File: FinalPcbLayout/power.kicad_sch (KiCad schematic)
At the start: 33 parts, among them Q1 NMOS, U4 AMS1117-3.3

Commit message: Part Finalization
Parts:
- added D4, D5: D_Schottky, symbol Device:D_Schottky
- added D7: RED, symbol Device:LED
- added J3: Barrel_Jack, Connector_BarrelJack:BarrelJack_GCT_DCJ200-10-A_Horizontal, symbol Connector:Barrel_Jack
- added Q4, Q5: PMOS, symbol Simulation_SPICE:PMOS
- added R23, R24: 10k, symbol Device:R_Small
- added R25: 100, symbol Device:R_Small
- D1: cost (none) -> .89; digikey_pn (none) -> SL42-E3/57TGITR-ND
- Q1: cost (none) -> .48; digikey_pn (none) -> 296-37193-6-ND
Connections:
- net +5V: now also D7.2 (A); no longer C1.2, C9.2, L1.1, U5.1 (BIAS), U5.12 (UVLO_)
- net GND: now also J3.2, R23.2, R24.2, R25.2
- net USB_Vin: now also Q4.1 (D); no longer C16.1, R13.1, U3.1 (PS/SYNC), U3.12 (VIN), U3.13 (VIN)
- new net: D7.1 (K), R25.1
- new net: D5.2 (A), Q4.2 (G), R24.1
- new net: D4.2 (A), Q5.2 (G), R23.1
- new net: J3.1, Q5.1 (D)
- new net V_in: C1.2, C16.1, C9.2, D4.1 (K), D5.1 (K), L1.1, Q4.3 (S), Q5.3 (S), R13.1, U3.1 (PS/SYNC), U3.12 (VIN), U3.13 (VIN), U5.1 (BIAS), U5.12 (UVLO_)
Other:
- moved on the sheet: C1, C10, C11, C2, C3, C4, C5, C6, C7, C8, C9, D1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

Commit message: Sim Disabled
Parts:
- C1, C10, C11, C16, C17, C18, C19, C2, C3, C4, C5, C6, C7, C8, C9, D1, D4, D5, D7, J3, L1, L2, Q1, Q4, Q5, R1, R10, R11, R12, R13, R2, R23, R24, R25, R3, R4, R5, R6, R7, U3, U4, U5: Cost (none) -> 0
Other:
- moved on the sheet: C10, C11, U4

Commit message: Update schematic with footprints for power delivery
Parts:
- C10, C16, C18, C19, C6: footprint Capacitor_SMD:C_0603_1608Metric -> Capacitor_SMD:C_0805_2012Metric
- C5: footprint Capacitor_SMD:C_0603_1608Metric -> Capacitor_SMD:C_0201_0603Metric
- C9: footprint Capacitor_SMD:C_0603_1608Metric -> Capacitor_SMD:C_0805_2012Metric; Cost 0 -> (uuid fabb1e82-3a32-4eed-b578-540d99c03e17)
- R3, R4: footprint Resistor_SMD:R_0603_1608Metric -> Resistor_SMD:R_1206_3216Metric
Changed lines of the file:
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@@
       (effects (font (size 1.27 1.27)) hide)
     )
-    (pin "2")
-    (pin "1")
+    (pin "1")
+    (pin "2")
     (instances
       (project "FinalPcbLayout"
@@
       (effects (font (size 1.27 1.27)) hide)
     )
-    (property "Datasheet" "~" (at 97.79 53.34 0)
+    (property "Datasheet" "" (at 97.79 53.34 0)
       (effects (font (size 1.27 1.27)) hide)
     )
@@
       (effects (font (size 1.27 1.27)) hide)
     )
+    (pin "1")
+    (pin "2")
     (pin "3")
-    (pin "1")
-    (pin "2")
     (instances
       (project "FinalPcbLayout"
@@
       (effects (font (size 1.27 1.27)) hide)
     )
-    (pin "2")
-    (pin "1")
+    (pin "1")
+    (pin "2")
     (instances
       (project "FinalPcbLayout"
@@
       (effects (font (size 1.27 1.27)) (justify right))
     )
-    (property "Footprint" "Resistor_SMD:R_0603_1608Metric" (at 217.424 78.486 90)
+    (property "Footprint" "Resistor_SMD:R_1206_3216Metric" (at 217.424 78.486 90)
       (effects (font (size 1.27 1.27)) hide)
     )
@@
       (effects (font (size 1.27 1.27)) (justify right))
     )
-    (property "Footprint" "Capacitor_SMD:C_0603_1608Metric" (at 232.7148 49.53 0)
+    (property "Footprint" "Capacitor_SMD:C_0201_0603Metric" (at 232.7148 49.53 0)
       (effects (font (size 1.27 1.27)) hide)
     )
@@
       (effects (font (size 1.27 1.27)) (justify left))
     )
-    (property "Footprint" "Capacitor_SMD:C_0603_1608Metric" (at 126.6952 144.78 0)
+    (property "Footprint" "Capacitor_SMD:C_0805_2012Metric" (at 126.6952 144.78 0)
       (effects (font (size 1.27 1.27)) hide)
     )
@@
       (effects (font (size 1.27 1.27)) (justify left))
     )
-    (property "Footprint" "Capacitor_SMD:C_0603_1608Metric" (at 260.0452 140.97 0)
+    (property "Footprint" "Capacitor_SMD:C_0805_2012Metric" (at 260.0452 140.97 0)
       (effects (font (size 1.27 1.27)) hide)
     )
@@
       (effects (font (size 1.27 1.27)) hide)
     )
-    (pin "2")
-    (pin "1")
+    (pin "1")
+    (pin "2")
     (instances
       (project "FinalPcbLayout"
@@
       (effects (font (size 1.27 1.27)))
     )
-    (property "Footprint" "Resistor_SMD:R_0603_1608Metric" (at 182.626 58.166 90)
+    (property "Footprint" "Resistor_SMD:R_1206_3216Metric" (at 182.626 58.166 90)
       (effects (font (size 1.27 1.27)) hide)
     )
@@
       (effects (font (size 1.27 1.27)) (justify left))
     )
-    (property "Footprint" "Capacitor_SMD:C_0603_1608Metric" (at 242.2652 140.97 0)
+    (property "Footprint" "Capacitor_SMD:C_0805_2012Metric" (at 242.2652 140.97 0)
       (effects (font (size 1.27 1.27)) hide)
     )
@@
       (effects (font (size 1.27 1.27)) (justify right))
     )
-    (property "Footprint" "Capacitor_SMD:C_0603_1608Metric" (at 192.0748 76.2 0)
+    (property "Footprint" "Capacitor_SMD:C_0805_2012Metric" (at 192.0748 76.2 0)
       (effects (font (size 1.27 1.27)) hide)
     )
@@
       (effects (font (size 1.27 1.27)) hide)
     )
+    (pin "1")
+    (pin "2")
     (pin "3")
-    (pin "1")
-    (pin "2")
     (instances
       (project "FinalPcbLayout"
@@
       (effects (font (size 1.27 1.27)) (justify left))
     )
-    (property "Footprint" "Capacitor_SMD:C_0603_1608Metric" (at 37.7952 132.08 0)
+    (property "Footprint" "Capacitor_SMD:C_0805_2012Metric" (at 37.7952 132.08 0)
       (effects (font (size 1.27 1.27)) hide)
     )
@@
       (effects (font (size 1.27 1.27)) hide)
     )
-    (pin "2")
-    (pin "1")
+    (pin "1")
+    (pin "2")
     (instances
       (project "FinalPcbLayout"
@@
       (effects (font (size 1.27 1.27)) (justify right))
     )
-    (property "Footprint" "Capacitor_SMD:C_0603_1608Metric" (at 89.2048 68.58 0)
+    (property "Footprint" "Capacitor_SMD:C_0805_2012Metric" (at 89.2048 68.58 0)
       (effects (font (size 1.27 1.27)) hide)
     )
@@
       (effects (font (size 1.27 1.27)) hide)
     )
-    (property "Cost" "0" (at 90.17 72.39 0)
-      (effects (font (size 1.27 1.27)) hide)
-    )
+    (property "Cost" "" (at 90.17 72.39 0)
+      (effects (font (size 1.27 1.27)) hide)
+    )

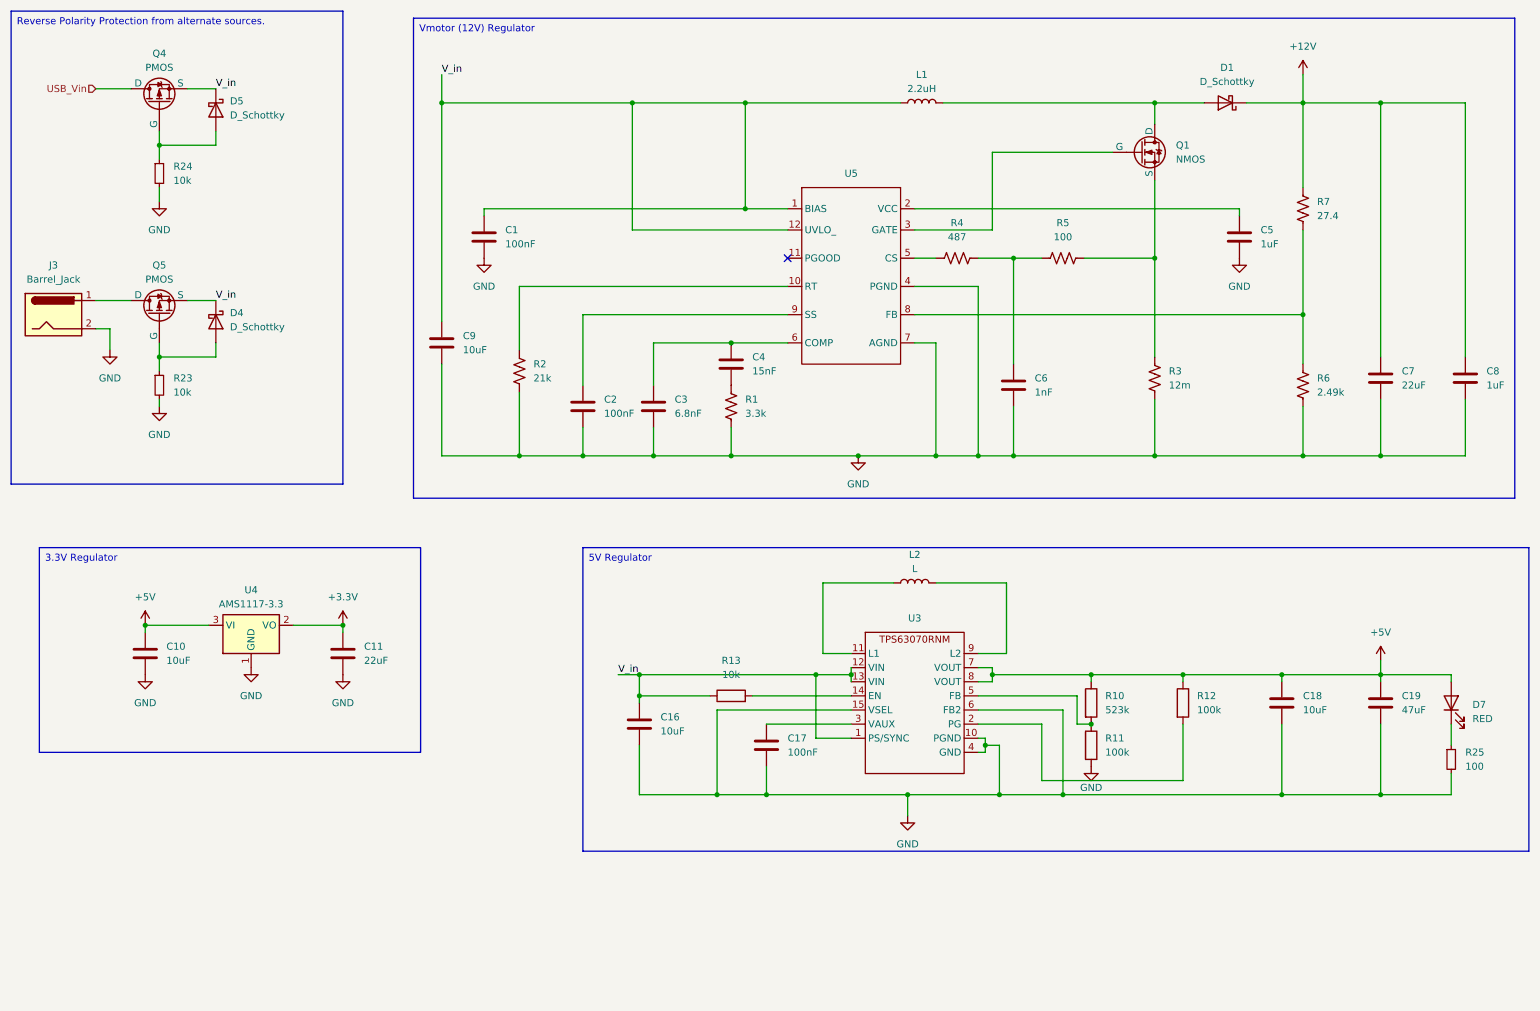
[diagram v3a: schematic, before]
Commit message: No ERC Errors
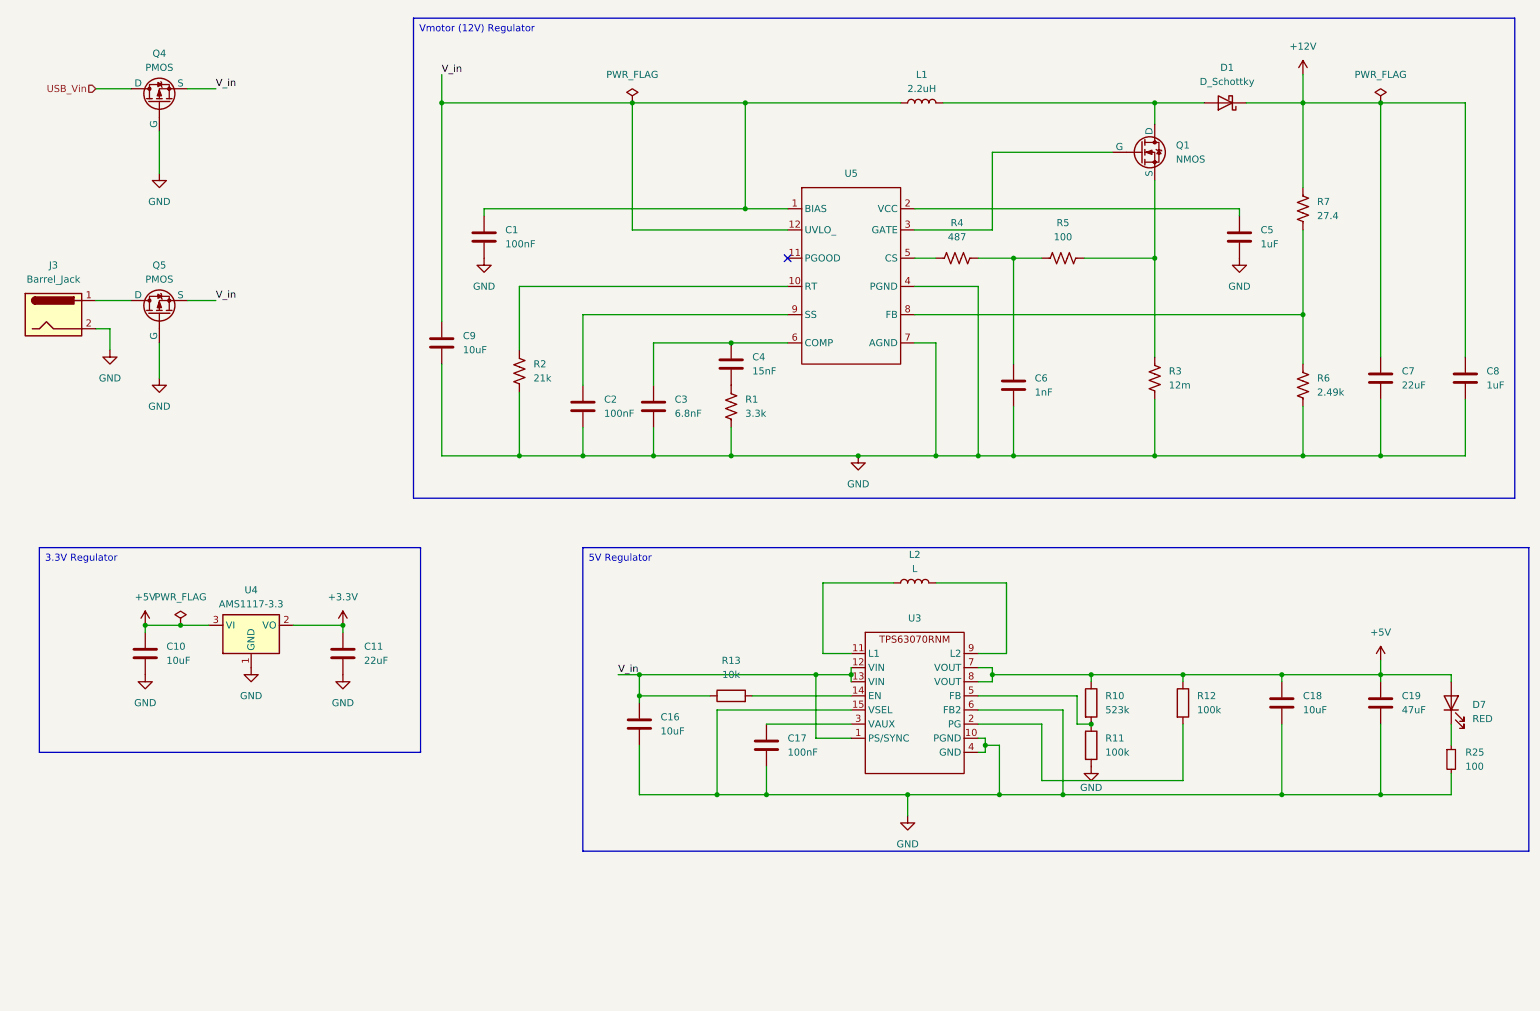
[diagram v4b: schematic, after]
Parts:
- removed D4, D5: D_Schottky, symbol Device:D_Schottky
- removed R23, R24: 10k, symbol Device:R_Small
- D7: footprint (none) -> LED_SMD:LED_0603_1608Metric
- Q4: footprint (none) -> Package_TO_SOT_SMD:Vishay_PowerPAK_SC70-6L_Single; Cost 0 -> (none); cost (none) -> .40; digikey_pn (none) -> 1727-PMV28XPEARTR-ND
- Q5: footprint (none) -> Package_TO_SOT_SMD:Vishay_PowerPAK_SC70-6L_Single; Cost 0 -> (none); cost (none) -> 0.4; digikey_pn (none) -> SIA461DJ-T1-GE3DKR-ND
- R25: footprint (none) -> Resistor_SMD:R_0805_2012Metric
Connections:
- net GND: now also Q4.2 (G), Q5.2 (G)

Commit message: All changes imported to PCB
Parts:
- Q4: symbol Simulation_SPICE:PMOS -> OSMI-parts:SIA461DJ-T1-GE3; cost .40 -> 0.4; digikey_pn 1727-PMV28XPEARTR-ND -> SIA461DJ-T1-GE3DKR-ND
- Q5: symbol Simulation_SPICE:PMOS -> OSMI-parts:SIA461DJ-T1-GE3
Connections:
- net GND: now also Q4.3 (G), Q5.3 (G); no longer Q4.2 (G), Q5.2 (G)
- net V_in: now also Q4.4 (S), Q5.4 (S); no longer Q4.3 (S), Q5.3 (S)
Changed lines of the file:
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@@
     )
   )
-  (symbol (lib_id "Simulation_SPICE:PMOS") (at 39.37 29.21 90) (unit 1)
+  (symbol (lib_id "OSMI-parts:SIA461DJ-T1-GE3") (at 39.37 29.21 90) (unit 1)
     (in_bom yes) (on_board yes) (dnp no) (fields_autoplaced)
     (property "Reference" "Q4" (at 39.37 20.32 90)
@@
       (effects (font (size 1.27 1.27)) hide)
     )
-    (property "Datasheet" "https://ngspice.sourceforge.io/docs/ngspice-manual.pdf" (at 52.07 29.21 0)
+    (property "Datasheet" "https://www.vishay.com/docs/63838/sia461dj.pdf" (at 52.07 29.21 0)
       (effects (font (size 1.27 1.27)) hide)
     )
@@
       (effects (font (size 1.27 1.27)) hide)
     )
-    (property "cost" ".40" (at 39.37 29.21 0)
+    (property "cost" "0.4" (at 39.37 29.21 0)
       (effects (font (size 1.27 1.27)) hide)
     )
@@
       (effects (font (size 1.27 1.27)) hide)
     )
-    (property "digikey_pn" "1727-PMV28XPEARTR-ND" (at 39.37 29.21 90)
-      (effects (font (size 1.27 1.27)) hide)
-    )
-    (pin "1")
-    (pin "2")
+    (property "digikey_pn" "SIA461DJ-T1-GE3DKR-ND" (at 39.37 29.21 90)
+      (effects (font (size 1.27 1.27)) hide)
+    )
+    (pin "1")
+    (pin "4")
     (pin "3")
     (instances
@@
     )
   )
-  (symbol (lib_id "Simulation_SPICE:PMOS") (at 39.37 67.31 90) (unit 1)
+  (symbol (lib_id "OSMI-parts:SIA461DJ-T1-GE3") (at 39.37 67.31 90) (unit 1)
     (in_bom yes) (on_board yes) (dnp no) (fields_autoplaced)
     (property "Reference" "Q5" (at 39.37 58.42 90)
@@
       (effects (font (size 1.27 1.27)) hide)
     )
-    (property "Datasheet" "https://ngspice.sourceforge.io/docs/ngspice-manual.pdf" (at 52.07 67.31 0)
+    (property "Datasheet" "https://www.vishay.com/docs/63838/sia461dj.pdf" (at 52.07 67.31 0)
       (effects (font (size 1.27 1.27)) hide)
     )
@@
     )
     (pin "1")
-    (pin "2")
+    (pin "4")
     (pin "3")
     (instances

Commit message: Routed UART Bridge
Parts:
- C5: footprint Capacitor_SMD:C_0201_0603Metric -> Capacitor_SMD:C_0603_1608Metric
- C7: footprint Capacitor_SMD:C_0603_1608Metric -> Capacitor_SMD:C_Elec_4x5.4
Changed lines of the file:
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@@
       (effects (font (size 1.27 1.27)) (justify right))
     )
-    (property "Footprint" "Capacitor_SMD:C_0603_1608Metric" (at 258.1148 74.93 0)
+    (property "Footprint" "Capacitor_SMD:C_Elec_4x5.4" (at 258.1148 74.93 0)
       (effects (font (size 1.27 1.27)) hide)
     )
@@
       (effects (font (size 1.27 1.27)) (justify right))
     )
-    (property "Footprint" "Capacitor_SMD:C_0201_0603Metric" (at 232.7148 49.53 0)
-      (effects (font (size 1.27 1.27)) hide)
-    )
+    (property "Footprint" "Capacitor_SMD:C_0603_1608Metric" (at 232.7148 49.53 0)
+      (effects (font (size 1.27 1.27)) hide)
+    )

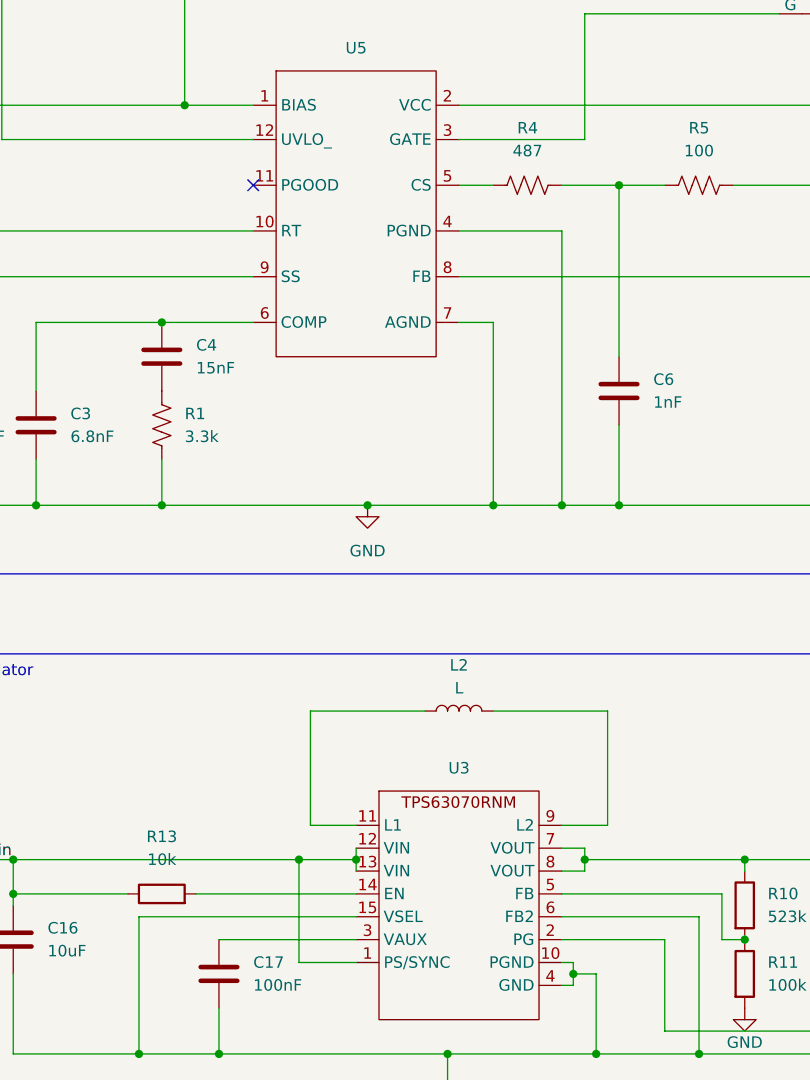
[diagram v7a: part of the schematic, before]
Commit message: More Schematic Label Updates
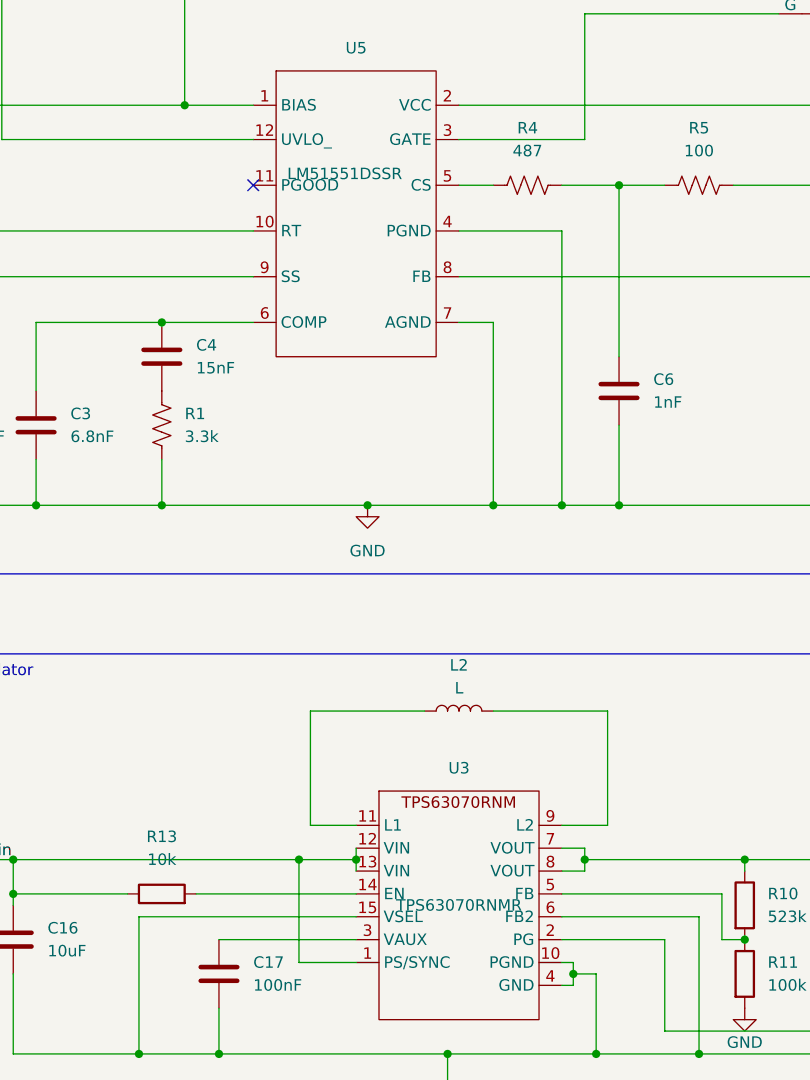
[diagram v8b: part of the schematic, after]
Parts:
- U3: value ~ -> TPS63070RNMR
- U5: value ~ -> LM51551DSSR
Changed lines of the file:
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@@
       (effects (font (size 1.27 1.27)))
     )
-    (property "Value" "~" (at 175.26 137.16 0)
+    (property "Value" "TPS63070RNMR" (at 175.26 137.16 0)
       (effects (font (size 1.27 1.27)))
     )
@@
       (effects (font (size 1.27 1.27)))
     )
-    (property "Value" "~" (at 162.56 55.88 0)
-      (effects (font (size 1.27 1.27)) hide)
+    (property "Value" "LM51551DSSR" (at 162.56 55.88 0)
+      (effects (font (size 1.27 1.27)))
     )
     (property "Footprint" "Package_SON:WSON-12-1EP_3x2mm_P0.5mm_EP1x2.65_ThermalVias" (at 162.56 55.88 0)
